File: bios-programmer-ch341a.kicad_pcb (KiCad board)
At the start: 2 copper layers, 50 x 56 mm, 48 parts, among them J1 USB_B_Micro, J4 -Banana-, J5 +Banana+, J6 ZIF16, J7 Conn_02x04_Counter_Clockwise, J8 Conn_02x04_Counter_Clockwise, Q1 SSM3J328R, Q2 SSM3J328R, Q3 SSM3J328R, Q4 SSM3J328R, SW1 RESET, U1 CH341A, U2 ISO6741, U3 ADuM1252, U4 TL431DBZ, Y1 12M

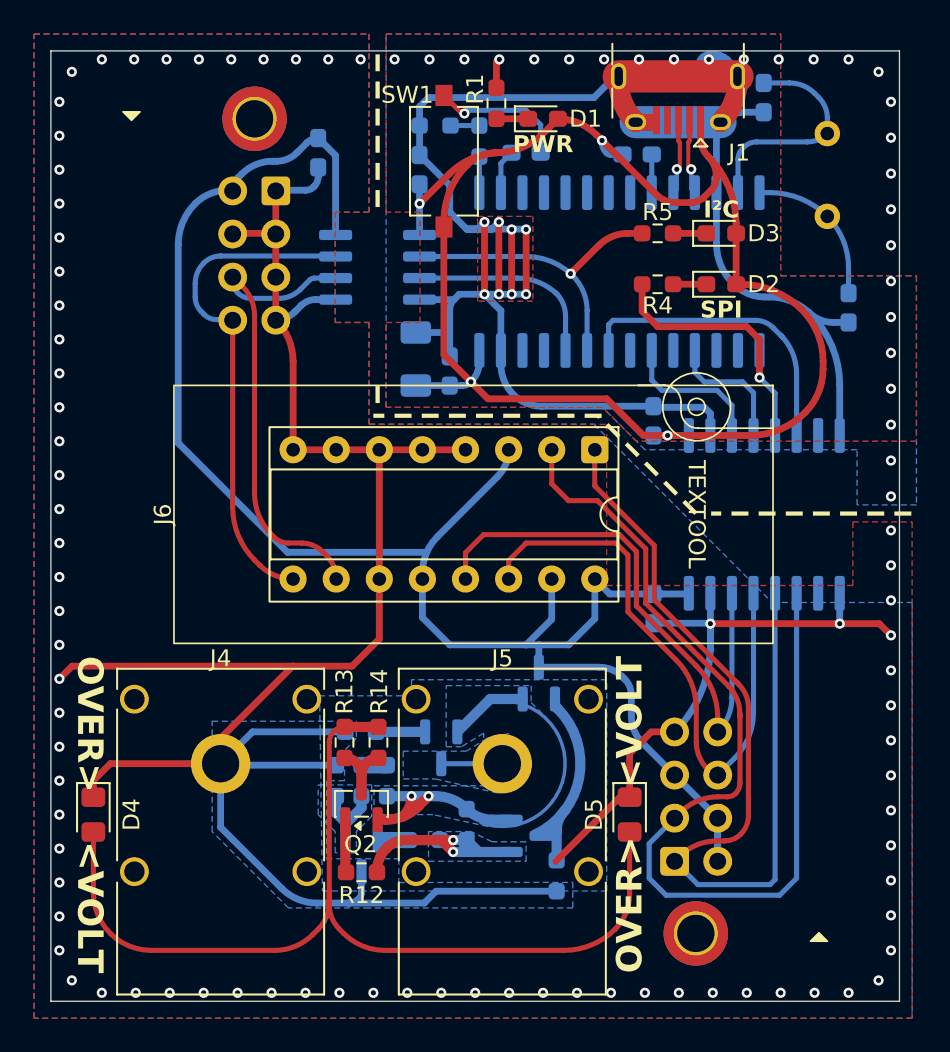
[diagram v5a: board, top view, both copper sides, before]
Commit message: SCH/PCB: 1% 5.6K resistor instead of 4.7K (1%) + 1K (5%)
Technically this would have worked as-is, since the 5% for the 1K results in
only a small change to the total resistance. The resulting voltage would be
(according to SPICE) between 5.3V and 5.49V, compared to 5.3V and 5.41V.

On the other hand I would expect a 1% resistor to also have a better tolerance
to temperature changes, which I did not simulate with actual resistor models.

The TL432 requires precise resistors if I want this OVP to work reliably.
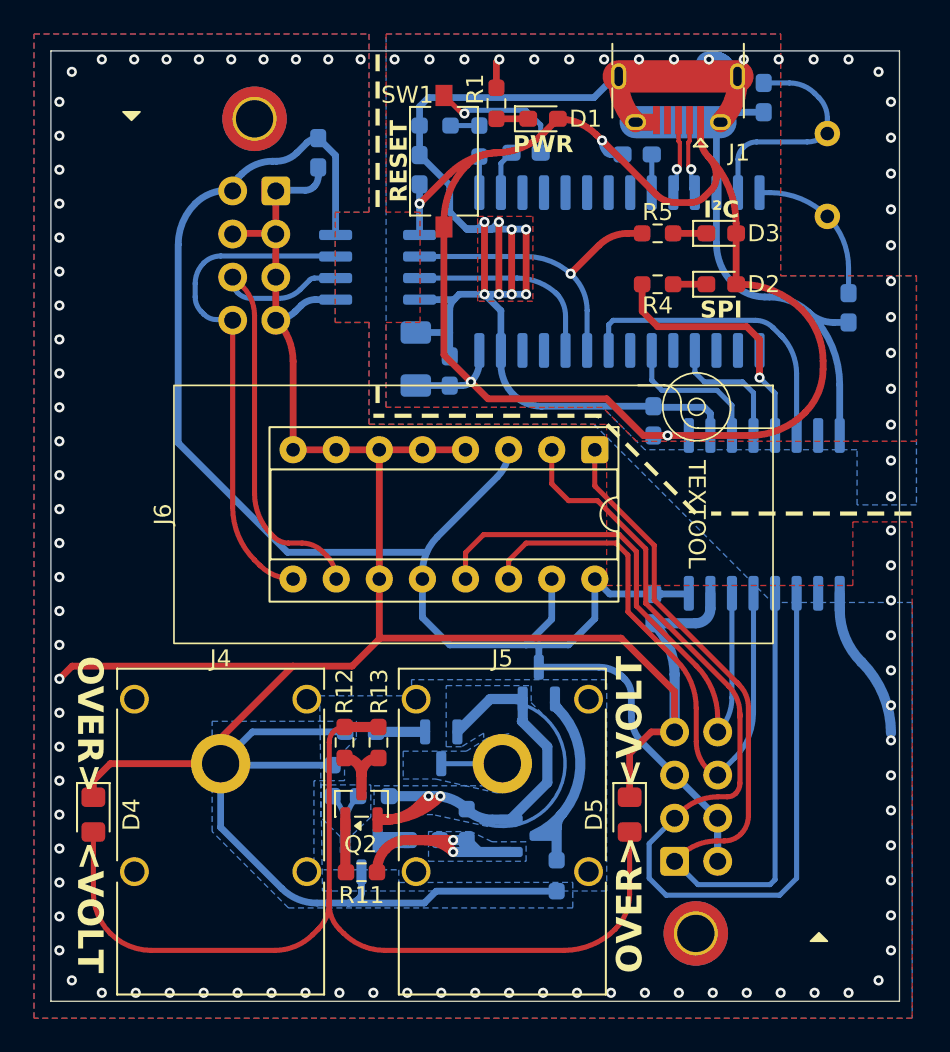
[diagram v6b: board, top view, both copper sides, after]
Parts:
- removed the R7 at (60.8, 73.0)
- R11: renamed from R12; value 1kΩ -> 10KΩ
- R12: renamed from R13; value 220Ω -> 200Ω
- R13: renamed from R14; value 220Ω -> 200Ω
- R14: renamed from R15; value 1kΩ -> 10KΩ
- R6: value 4k7Ω -> 10KΩ
- R7: renamed from R8; value 4k7Ω -> 5k6Ω
- U4: value TL431DBZ -> TL432DBZ
- Y1: value 12M -> 12MHz
- moved R7 1.16 mm to (60.0, 73.9), turned to 0 degrees
- moved R8 0.20 mm to (57.6, 73.0)
- renumbered R11 to R10, R9 to R8, R10 to R9
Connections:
- R7 pad 2: Net-(R7-Pad1) -> /VSW
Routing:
- net /VSW: track 17.0 -> 28.1 mm
- net GNDD: track 453.1 -> 462.4 mm, vias 76 -> 74
- net Net-(R7-Pad1): track 1.50 -> 0.00 mm
- net /REF431: track 5.80 -> 4.77 mm
- net /VG_AUX: track 14.4 -> 15.2 mm

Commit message: PCB: moving stuff; more GND; pcb all is well; before I increase clearance TODO
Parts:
- C4, C5: moved to F.Cu
- moved SW1 5.85 mm to (70.0, 36.2), turned to 180 degrees
- moved R4 5.47 mm to (81.8, 45.8), turned to 180 degrees
- moved R3 5.36 mm to (69.0, 34.4), turned to 0 degrees
- moved R1 5.12 mm to (62.2, 32.0), turned to 180 degrees
- moved D1 4.70 mm to (65.8, 32.0)
- moved D2 3.20 mm to (78.0, 45.8), turned to 180 degrees
- moved D3 2.85 mm to (78.0, 42.1)
- moved R5 2.85 mm to (74.2, 42.1)
- moved C5 2.72 mm to (65.2, 46.2)
- moved C4 1.53 mm to (63.5, 47.0)
- moved R8 1.35 mm to (56.7, 74.0), turned to 0 degrees
- moved C7 1.30 mm to (62.4, 38.2), turned to 0 degrees
- moved R6 0.75 mm to (60.0, 70.1)
- moved C3 0.25 mm to (69.0, 36.2)
- moved C6 0.15 mm to (75.5, 36.2)
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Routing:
- net GND: track 239.1 -> 223.7 mm, vias 35 -> 28
- net /CS: track 16.8 -> 7.93 mm
- net VBUS: track 93.5 -> 86.4 mm
- net Net-(Q1-G): track 2.89 -> 1.83 mm
- net /RST: track 8.21 -> 7.51 mm
- net GNDD: track 462.4 -> 461.7 mm
- net /SDA: track 19.0 -> 18.5 mm, vias 1 -> 2
- net /SCL: track 11.9 -> 12.4 mm, vias 0 -> 2
- removed copper zone on F.Cu, net GND

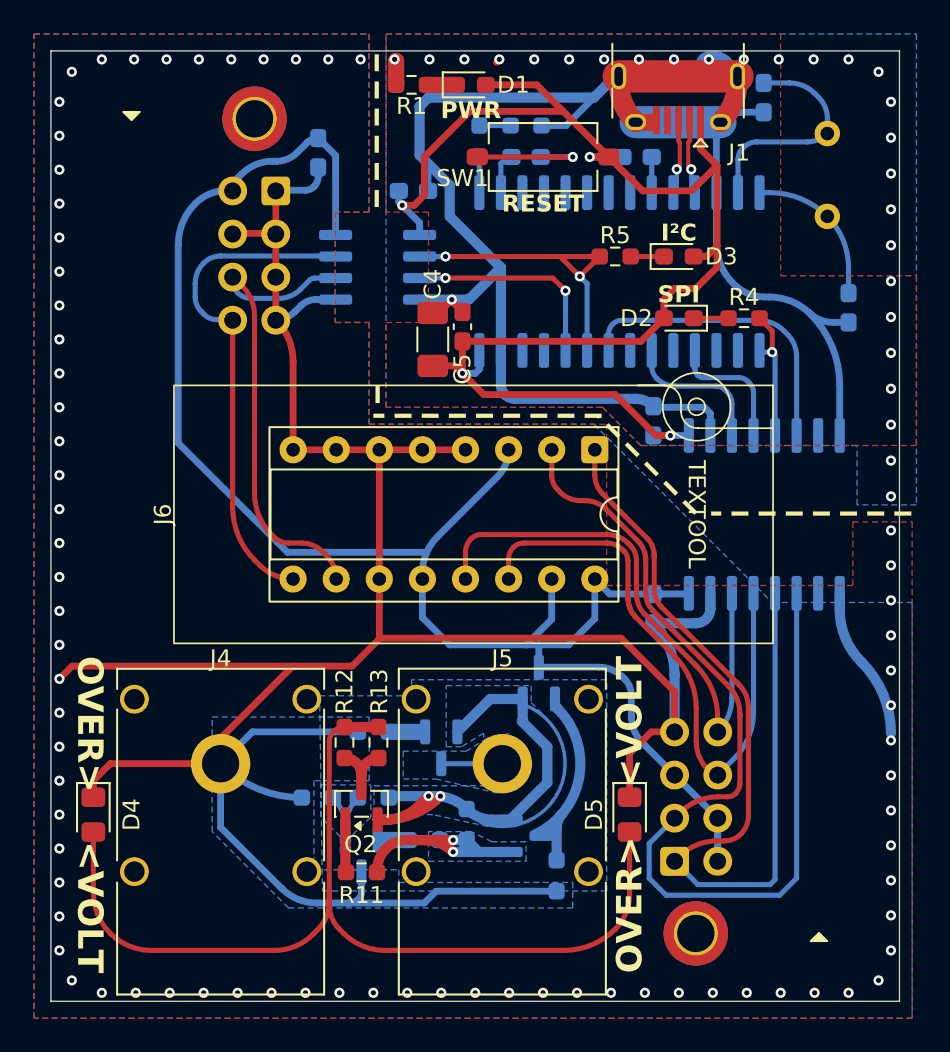
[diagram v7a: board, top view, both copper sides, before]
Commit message: PCB increase clearances, no need to be tight; increased track widths; nets for all non-default?
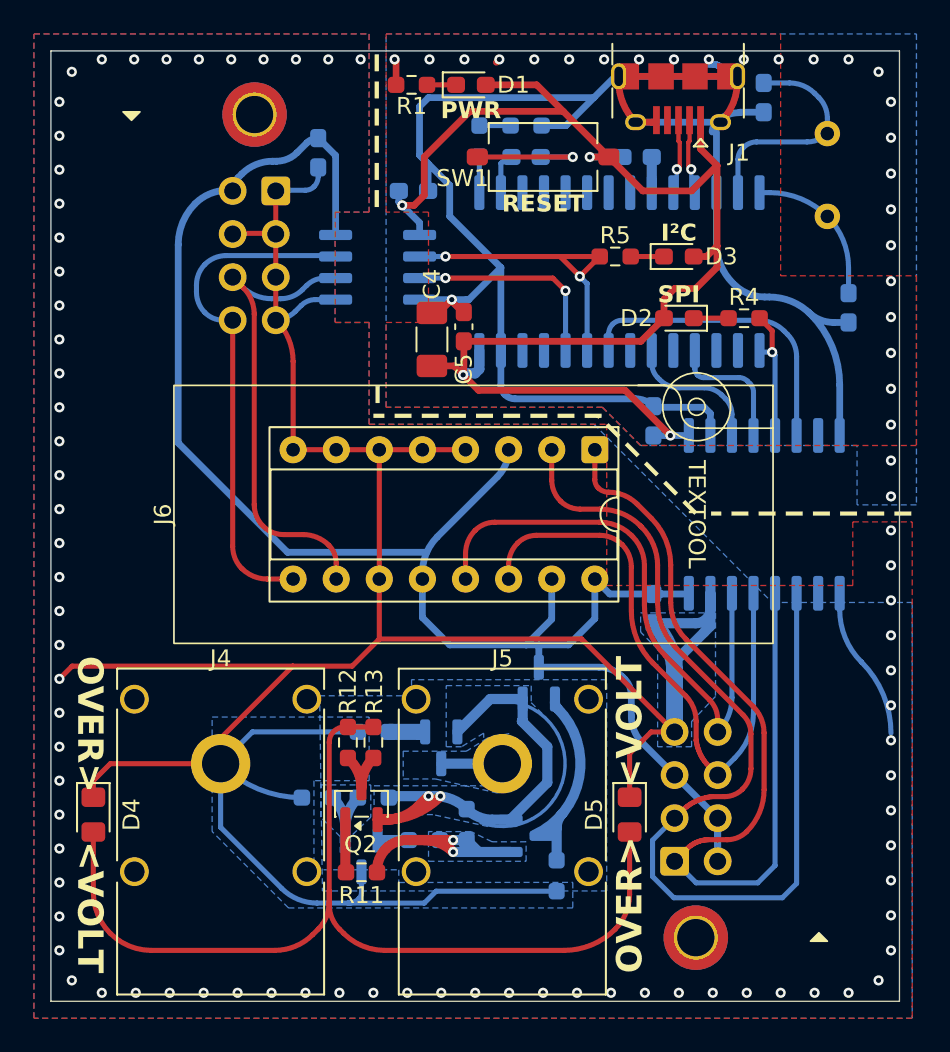
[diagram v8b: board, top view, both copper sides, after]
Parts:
- moved R13 0.30 mm to (60.0, 70.8)
- moved H1 0.25 mm to (53.0, 33.8)
- moved H2 0.25 mm to (79.0, 82.2)
- moved R12 0.20 mm to (58.5, 70.8)
- moved C5 0.08 mm to (65.3, 46.2)
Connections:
- net /REF431 renamed /431REF
- net Net-(Q1-G) renamed /REVI_PROT
- net Net-(Q2-D) renamed /Q2_S
- net Net-(Q2-G) renamed /Q2_G
- net Net-(U4-K) renamed /431AN
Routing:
- net GNDD: track 461.7 -> 469.3 mm
- net /MOSI_I: track 33.2 -> 34.9 mm
- net /MOSI: track 8.72 -> 7.54 mm
- net /CS_I: track 53.6 -> 54.8 mm
- net /MISO_I: track 59.4 -> 60.5 mm
- net /CLK_I: track 34.5 -> 35.5 mm
- net /SDA_I: track 30.8 -> 30.0 mm
